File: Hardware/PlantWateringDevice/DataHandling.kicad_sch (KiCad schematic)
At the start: 6 parts, among them J5 Conn_02x03_Odd_Even, SW7 SW_DIP_x02, U3 PIC10F200-IOT

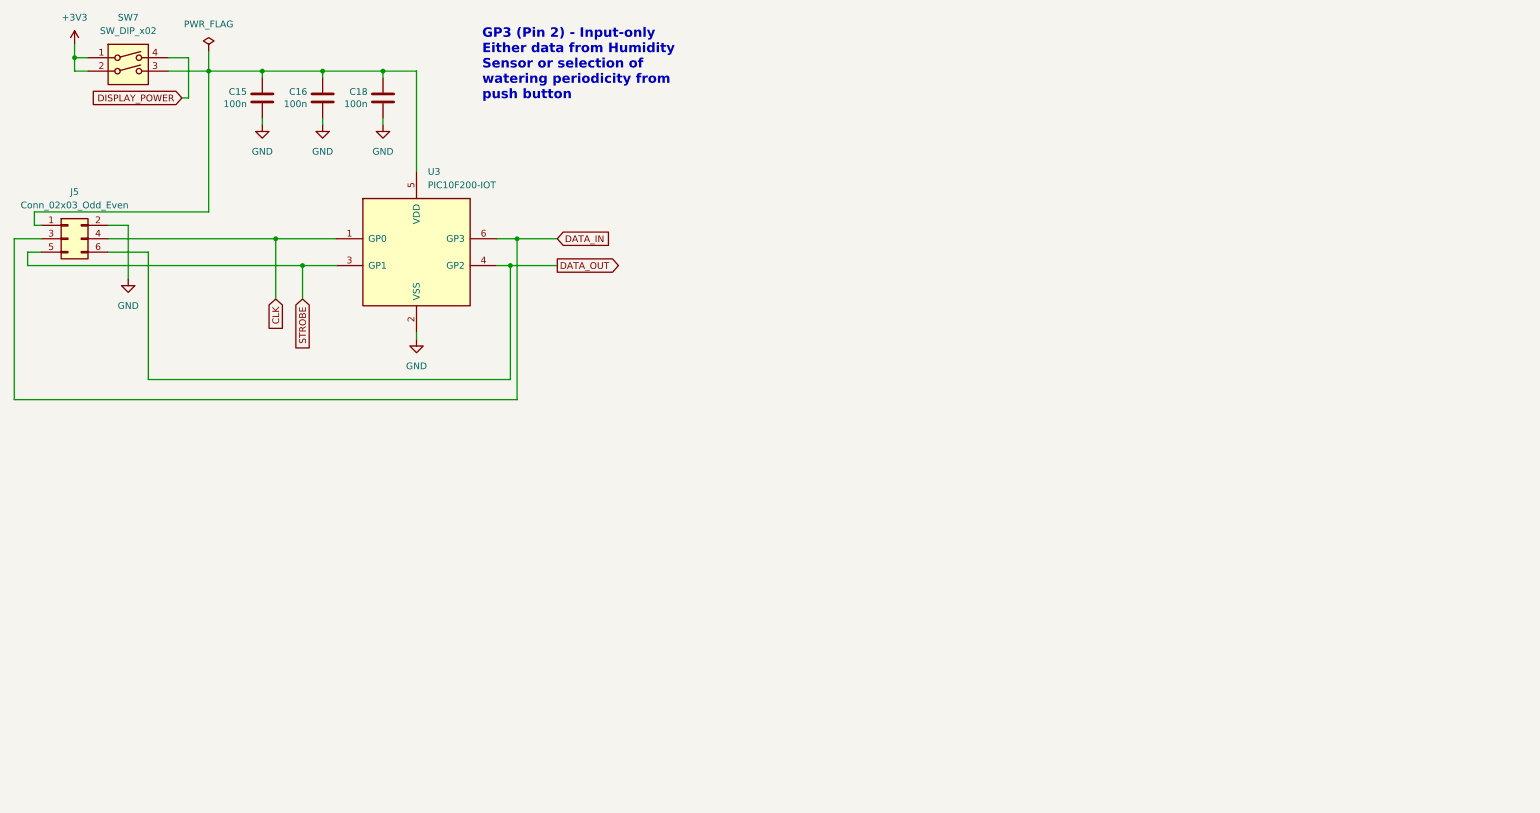
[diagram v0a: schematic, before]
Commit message: circuit simplification
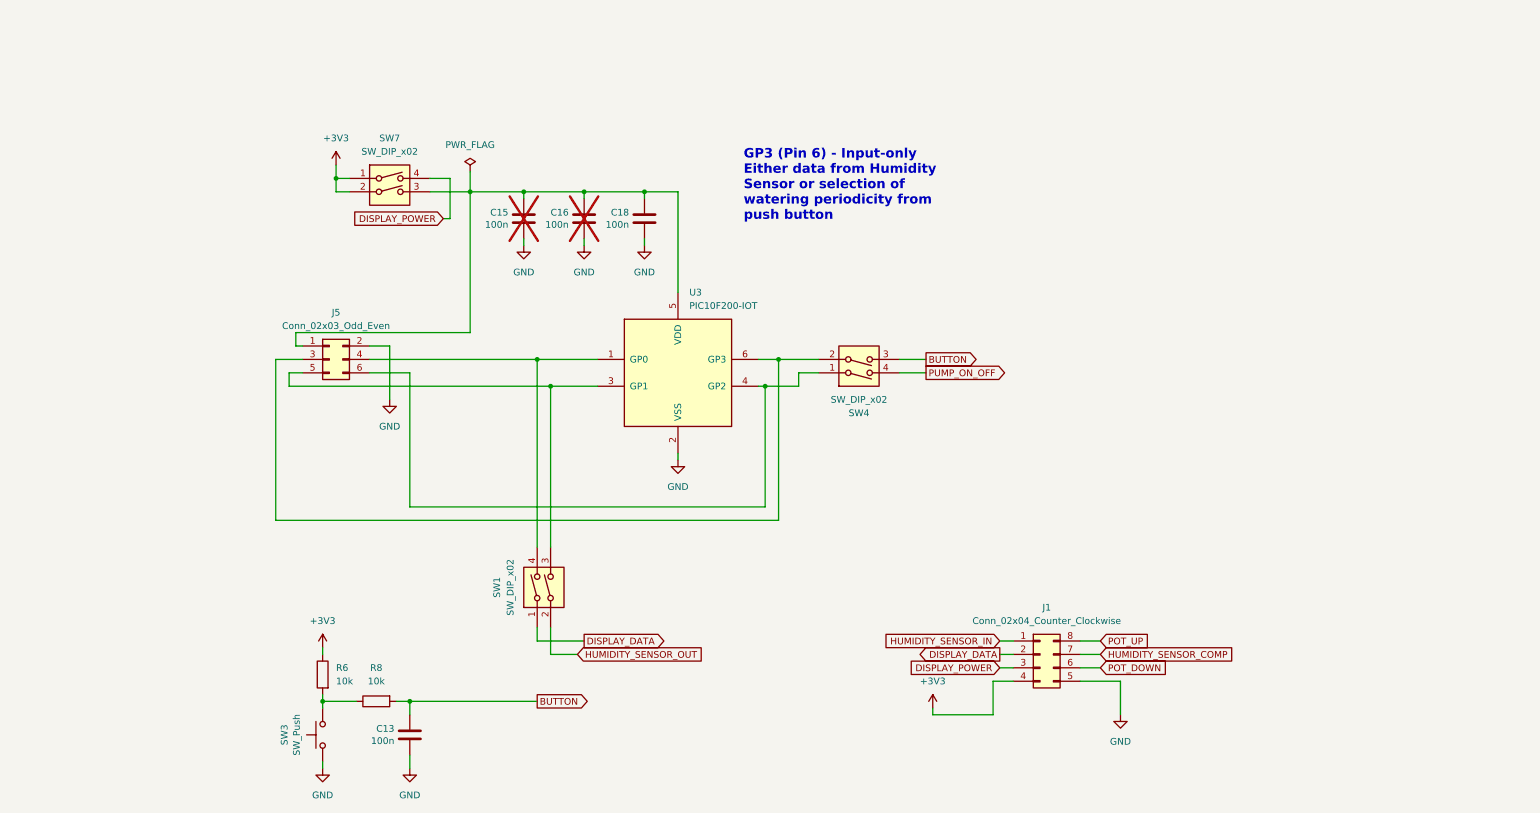
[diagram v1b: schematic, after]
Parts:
- added C13: 100n, Capacitor_SMD:C_0805_2012Metric, symbol Device:C
- added J1: Conn_02x04_Counter_Clockwise, Connector_PinHeader_2.54mm:PinHeader_2x04_P2.54mm_Vertical, symbol Connector_Generic:Conn_02x04_Counter_Clockwise
- added R6, R8: 10k, Resistor_SMD:R_0805_2012Metric, symbol Device:R
- added SW1, SW4: SW_DIP_x02, Package_DIP:DIP-4_W7.62mm, symbol Switch:SW_DIP_x02
- added SW3: SW_Push, Button_Switch_SMD:SW_SPST_PTS645, symbol Switch:SW_Push
- C15, C16: now not fitted
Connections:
- net +3V3: now also J1.4 (Pin_4), R6.1
- net DISPLAY_POWER: now also J1.3 (Pin_3)
- net GND: now also C13.2, J1.5 (Pin_5), SW3.1
- net CLK: no longer names the net of J5.4 (Pin_4), U3.1 (GP0)
- net CLK: now also SW1.4
- net DATA_IN: no longer names the net of J5.3 (Pin_3), U3.6 (GP3)
- net DATA_IN: now also SW4.2
- net DATA_OUT: no longer names the net of J5.6 (Pin_6), U3.4 (GP2)
- net DATA_OUT: now also SW4.1
- net STROBE: no longer names the net of J5.5 (Pin_5), U3.3 (GP1)
- net STROBE: now also SW1.3
- new net: R6.2, R8.1, SW3.2
- new net BUTTON: C13.1, R8.2, SW4.3
- new net DISPLAY_DATA: J1.2 (Pin_2), SW1.1
- new net HUMIDITY_SENSOR_COMP: J1.7 (Pin_7)
- new net HUMIDITY_SENSOR_IN: J1.1 (Pin_1)
- new net HUMIDITY_SENSOR_OUT: SW1.2
- new net POT_DOWN: J1.6 (Pin_6)
- new net POT_UP: J1.8 (Pin_8)
- new net PUMP_ON_OFF: SW4.4
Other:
- note added: "GP3 (Pin 6) - Input-only Either data from Humidity Sensor or selection of watering periodicity from push button"
- note removed: "GP3 (Pin 2) - Input-only Either data from Humidity Sensor or selection of watering periodicity from push button"
- moved on the sheet: C18, J5, SW7, U3

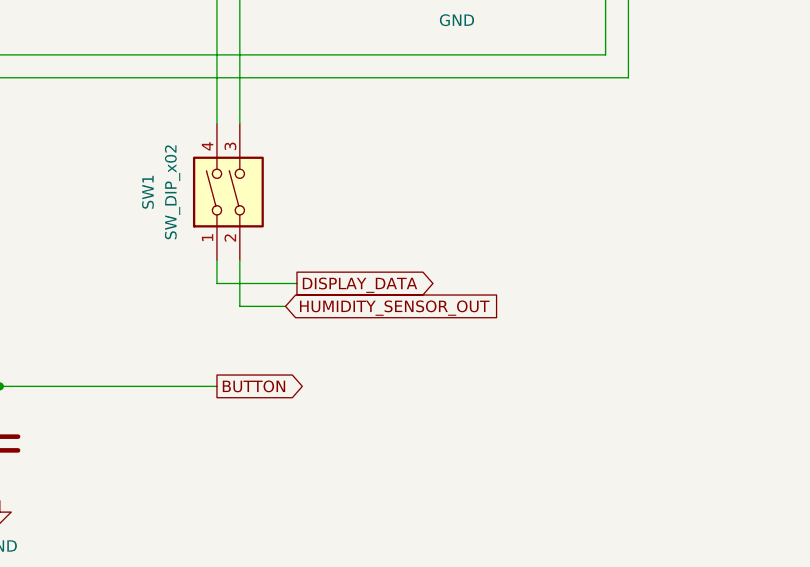
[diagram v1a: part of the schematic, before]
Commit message: use openscad for param modeling
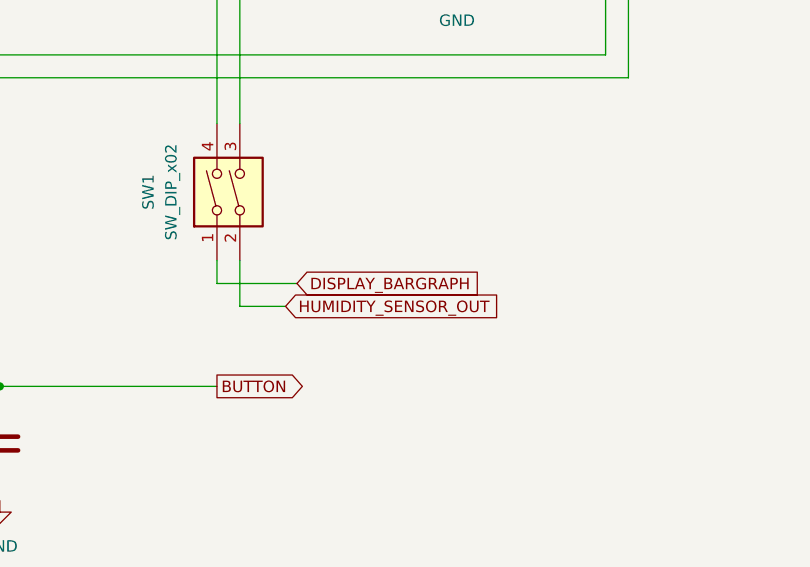
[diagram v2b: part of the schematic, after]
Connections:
- net DISPLAY_DATA: no longer SW1.1
- new net DISPLAY_BARGRAPH: SW1.1
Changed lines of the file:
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@@
 		)
 	)
-	(global_label "DISPLAY_DATA"
-		(shape output)
+	(global_label "DISPLAY_BARGRAPH"
+		(shape input)
 		(at 135.89 134.62 0)
 		(fields_autoplaced yes)
@@
 		)
 		(property "Intersheetrefs" "${INTERSHEET_REFS}"
-			(at 151.8172 134.62 0)
+			(at 157.2601 134.62 0)
 			(effects
 				(font

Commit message: improvements after eric's comments
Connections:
- net +3V3 renamed VCC

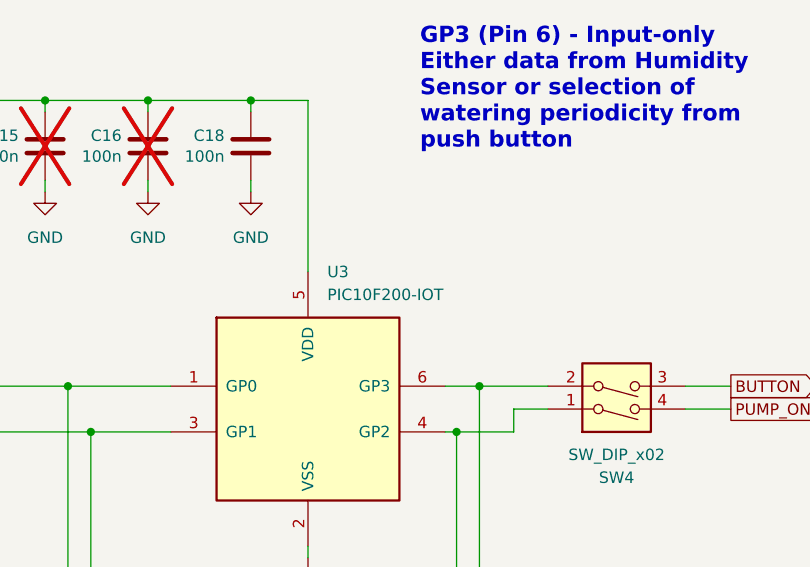
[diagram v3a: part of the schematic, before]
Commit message: fixes before sending pcb and 3d model to production
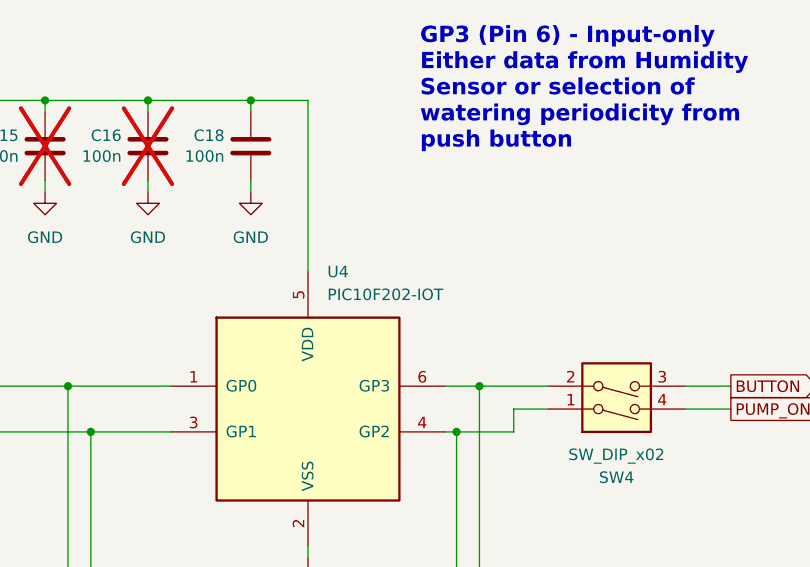
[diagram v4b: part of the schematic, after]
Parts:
- removed U3: PIC10F200-IOT, Package_TO_SOT_SMD:SOT-23-6, symbol MCU_Microchip_PIC10:PIC10F200-IOT
- added U4: PIC10F202-IOT, Package_TO_SOT_SMD:SOT-23-6, symbol MCU_Microchip_PIC10:PIC10F202-IOT
- SW3: footprint Button_Switch_SMD:SW_SPST_PTS645 -> Button_Switch_SMD:SW_SPST_PTS645Sx43SMTR92
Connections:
- net GND: now also U4.2 (VSS)
- net at J5.5 (Pin_5), SW1.3: now also U4.3 (GP1)
- net at J5.4 (Pin_4), SW1.4: now also U4.1 (GP0)
- net at C15.1, C16.1, C18.1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: now also U4.5 (VDD)
- net at J5.6 (Pin_6), SW4.1: now also U4.4 (GP2)
- net at J5.3 (Pin_3), SW4.2: now also U4.6 (GP3)
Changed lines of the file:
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@@
+	)
+	(symbol
+		(lib_id "MCU_Microchip_PIC10:PIC10F202-IOT")
+		(at 153.67 83.82 0)
+		(unit 1)
+		(exclude_from_sim no)
+		(in_bom yes)
+		(on_board yes)
+		(dnp no)
+		(fields_autoplaced yes)
+		(property "Reference" "U4"
+			(at 155.8133 68.58 0)
+			(effects
+				(font
+					(size 1.27 1.27)
+				)
+				(justify left)
+			)
+		)
+		(property "Value" "PIC10F202-IOT"
+			(at 155.8133 71.12 0)
+			(effects
+				(font
+					(size 1.27 1.27)
+				)
+				(justify left)
+			)
+		)
+		(property "Footprint" "Package_TO_SOT_SMD:SOT-23-6"
+			(at 154.94 67.31 0)
+			(effects
+				(font
+					(size 1.27 1.27)
+					(italic yes)
+				)
+				(justify left)
+				(hide yes)
+			)
+		)
+		(property "Datasheet" "http://ww1.microchip.com/downloads/en/DeviceDoc/41239D.pdf"
+			(at 153.67 83.82 0)
+			(effects
+				(font
+					(size 1.27 1.27)
+				)
+				(hide yes)
+			)
+		)
+		(property "Description" "512W Flash, 24B SRAM, SOT-23-6"
+			(at 153.67 83.82 0)
+			(effects
+				(font
+					(size 1.27 1.27)
+				)
+				(hide yes)
+			)
+		)
+		(pin "2"
+		)
+		(pin "5"
+		)
+		(pin "3"
+		)
+		(pin "6"
+		)
+		(pin "1"
+		)
+		(pin "4"
+		)
+		(instances
+			(project ""
+				(path "/1ef241b3-83d7-48ae-bcca-b7d0eea44e63/774c5e66-df25-4246-b332-f6d1db12f11e"
+					(reference "U4")
+					(unit 1)
+				)
+			)
+		)
 	)
 	(symbol
@@
 			)
 		)
-		(property "Footprint" "Button_Switch_SMD:SW_SPST_PTS645"
+		(property "Footprint" "Button_Switch_SMD:SW_SPST_PTS645Sx43SMTR92"
 			(at 81.28 152.4 0)
 			(effects
@@
 					(unit 1)
 				)
-			)
-		)
-	)
-	(symbol
-		(lib_id "MCU_Microchip_PIC10:PIC10F200-IOT")
-		(at 153.67 83.82 0)
-		(unit 1)
-		(exclude_from_sim no)
-		(in_bom yes)
-		(on_board yes)
-		(dnp no)
-		(fields_autoplaced yes)
-		(property "Reference" "U3"
-			(at 155.8133 68.58 0)
-			(effects
-				(font
-					(size 1.27 1.27)
-				)
-				(justify left)
-			)
-		)
-		(property "Value" "PIC10F200-IOT"
-			(at 155.8133 71.12 0)
-			(effects
-				(font
-					(size 1.27 1.27)
-				)
-				(justify left)
-			)
-		)
-		(property "Footprint" "Package_TO_SOT_SMD:SOT-23-6"
-			(at 154.94 67.31 0)
-			(effects
-				(font
-					(size 1.27 1.27)
-					(italic yes)
-				)
-				(justify left)
-				(hide yes)
-			)
-		)
-		(property "Datasheet" "http://ww1.microchip.com/downloads/en/DeviceDoc/41239D.pdf"
-			(at 153.67 83.82 0)
-			(effects
-				(font
-					(size 1.27 1.27)
-				)
-				(hide yes)
-			)
-		)
-		(property "Description" "256W Flash, 16B SRAM, SOT-23-6"
-			(at 153.67 83.82 0)
-			(effects
-				(font
-					(size 1.27 1.27)
-				)
-				(hide yes)
-			)
-		)
-		(pin "1"
-		)
-		(pin "2"
-		)
-		(pin "6"
-		)
-		(pin "4"
-		)
-		(pin "5"
-		)
-		(pin "3"
-		)
-		(instances
-			(project "PlantWateringDevice"
-				(path "/1ef241b3-83d7-48ae-bcca-b7d0eea44e63/774c5e66-df25-4246-b332-f6d1db12f11e"
-					(reference "U3")
-					(unit 1)
-				)

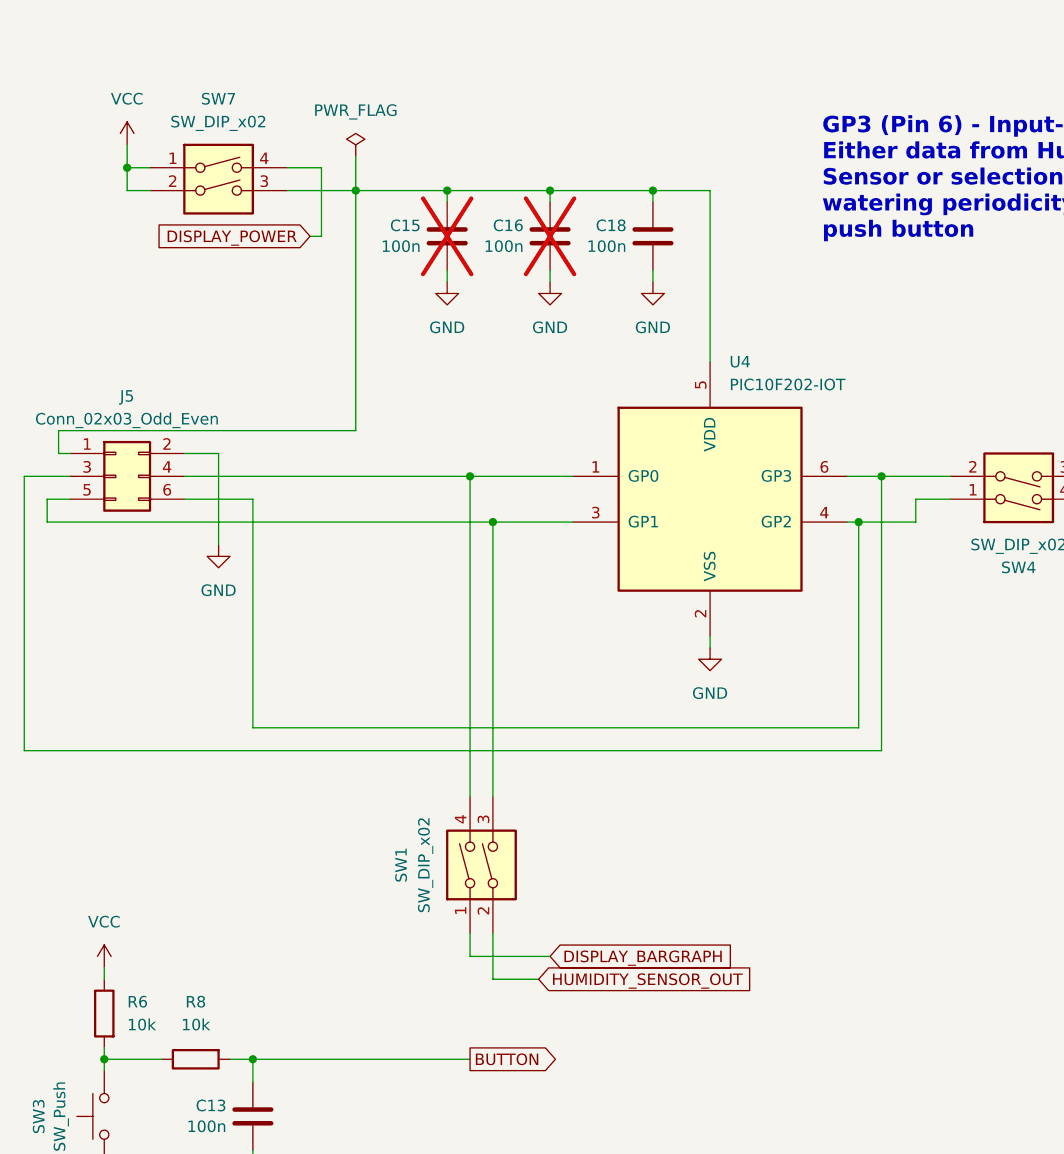
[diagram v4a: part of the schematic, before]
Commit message: README.md cleanup
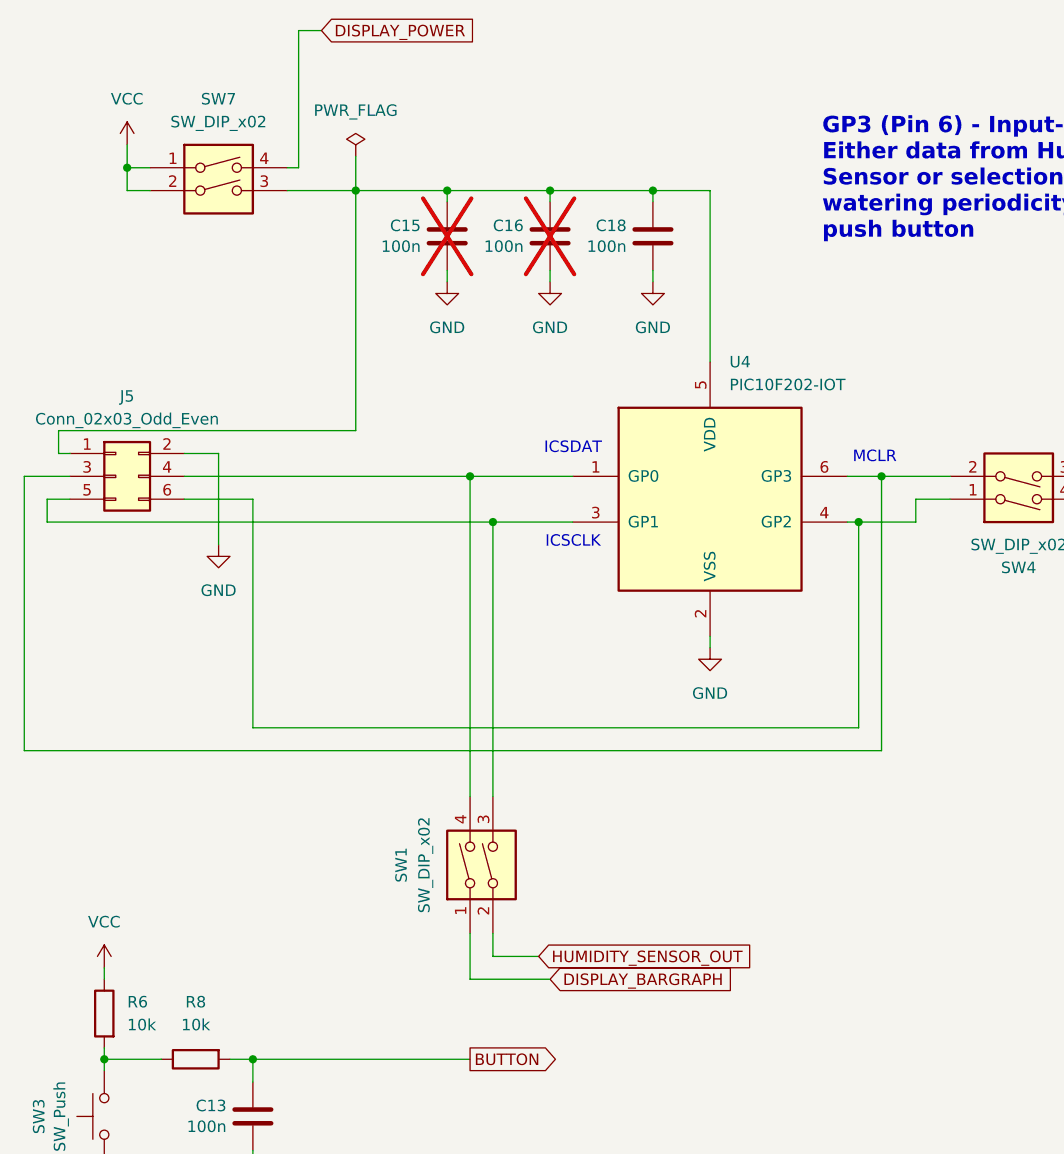
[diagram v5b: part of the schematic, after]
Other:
- note added: "ICSCLK"
- note added: "ICSDAT"
- note added: "MCLR"
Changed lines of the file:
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@@
 	(generator_version "9.0")
 	(paper "A4")
+	(text "ICSCLK"
+		(exclude_from_sim no)
+		(at 138.43 88.646 0)
+		(effects
+			(font
+				(size 1.27 1.27)
+			)
+		)
+	)
 	(text "GP3 (Pin 6) - Input-only\nEither data from Humidity\nSensor or selection of\nwatering periodicity from\npush button"
 		(exclude_from_sim no)
@@
 		)
 	)
+	(text "ICSDAT"
+		(exclude_from_sim no)
+		(at 138.43 78.232 0)
+		(effects
+			(font
+				(size 1.27 1.27)
+			)
+		)
+	)
+	(text "MCLR"
+		(exclude_from_sim no)
+		(at 171.958 79.248 0)
+		(effects
+			(font
+				(size 1.27 1.27)
+			)
+		)
+	)
 	(junction
 		(at 102.87 146.05)
@@
 	(wire
 		(pts
-			(xy 129.54 137.16) (xy 134.62 137.16)
+			(xy 129.54 134.62) (xy 134.62 134.62)
 		)
 		(stroke
@@
 	(wire
 		(pts
-			(xy 127 134.62) (xy 127 132.08)
+			(xy 127 137.16) (xy 127 132.08)
 		)
 		(stroke
@@
 	(wire
 		(pts
-			(xy 135.89 134.62) (xy 127 134.62)
+			(xy 135.89 137.16) (xy 127 137.16)
 		)
 		(stroke
@@
 	(wire
 		(pts
-			(xy 110.49 46.99) (xy 110.49 54.61)
-		)
-		(stroke
-			(width 0)
-			(type default)
-		)
-	)
-	(wire
-		(pts
-			(xy 109.22 54.61) (xy 110.49 54.61)
+			(xy 107.95 31.75) (xy 107.95 46.99)
 		)
 		(stroke
@@
 	(wire
 		(pts
-			(xy 106.68 46.99) (xy 110.49 46.99)
+			(xy 106.68 46.99) (xy 107.95 46.99)
 		)
 		(stroke
@@
 	(wire
 		(pts
-			(xy 129.54 132.08) (xy 129.54 137.16)
+			(xy 129.54 132.08) (xy 129.54 134.62)
 		)
 		(stroke
@@
 		(pts
 			(xy 135.89 49.53) (xy 135.89 50.8)
+		)
+		(stroke
+			(width 0)
+			(type default)
+		)
+	)
+	(wire
+		(pts
+			(xy 107.95 31.75) (xy 110.49 31.75)
 		)
 		(stroke
@@
 	(global_label "DISPLAY_POWER"
 		(shape input)
-		(at 109.22 54.61 180)
+		(at 110.49 31.75 0)
 		(fields_autoplaced yes)
 		(effects
@@
 				(size 1.27 1.27)
 			)
-			(justify right)
+			(justify left)
 		)
 		(property "Intersheetrefs" "${INTERSHEET_REFS}"
-			(at 91.2367 54.61 0)
+			(at 128.4733 31.75 0)
 			(effects
 				(font
 					(size 1.27 1.27)
 				)
-				(justify right)
+				(justify left)
 				(hide yes)
 			)
@@
 	(global_label "HUMIDITY_SENSOR_OUT"
 		(shape input)
-		(at 134.62 137.16 0)
+		(at 134.62 134.62 0)
 		(fields_autoplaced yes)
 		(effects
@@
 		)
 		(property "Intersheetrefs" "${INTERSHEET_REFS}"
-			(at 159.3162 137.16 0)
+			(at 159.3162 134.62 0)
 			(effects
 				(font
@@
 	(global_label "DISPLAY_BARGRAPH"
 		(shape input)
-		(at 135.89 134.62 0)
+		(at 135.89 137.16 0)
 		(fields_autoplaced yes)
 		(effects
@@
 		)
 		(property "Intersheetrefs" "${INTERSHEET_REFS}"
-			(at 157.2601 134.62 0)
+			(at 157.2601 137.16 0)
 			(effects
 				(font
